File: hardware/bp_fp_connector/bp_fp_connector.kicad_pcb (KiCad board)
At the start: 2 copper layers, 26.3 x 100 mm, 0 parts

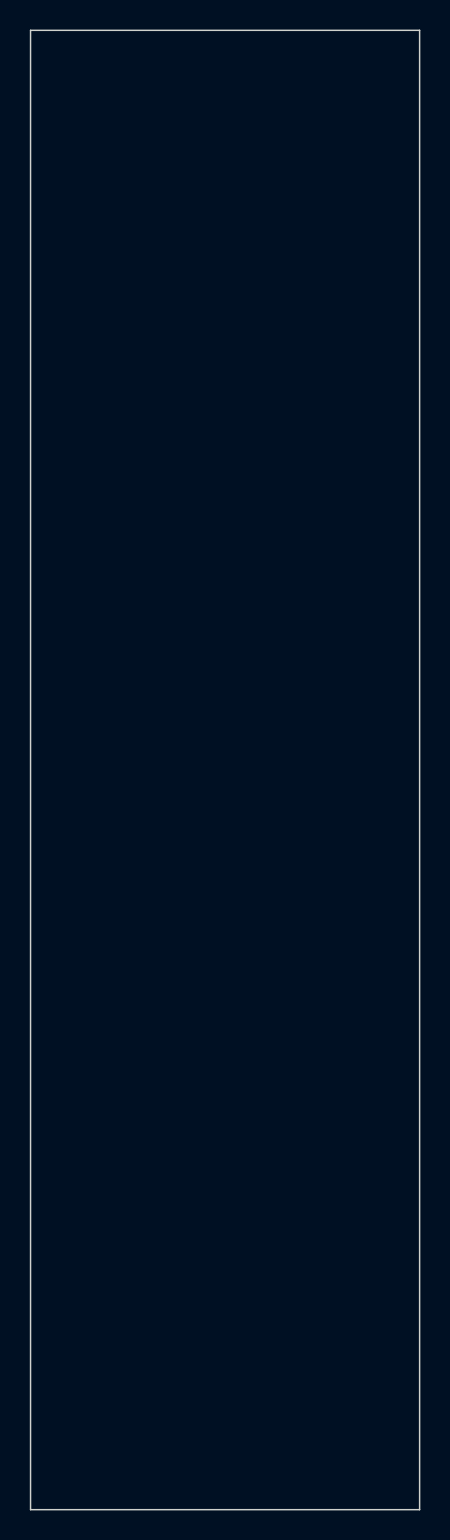
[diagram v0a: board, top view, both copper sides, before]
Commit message: front panel - backplane connector
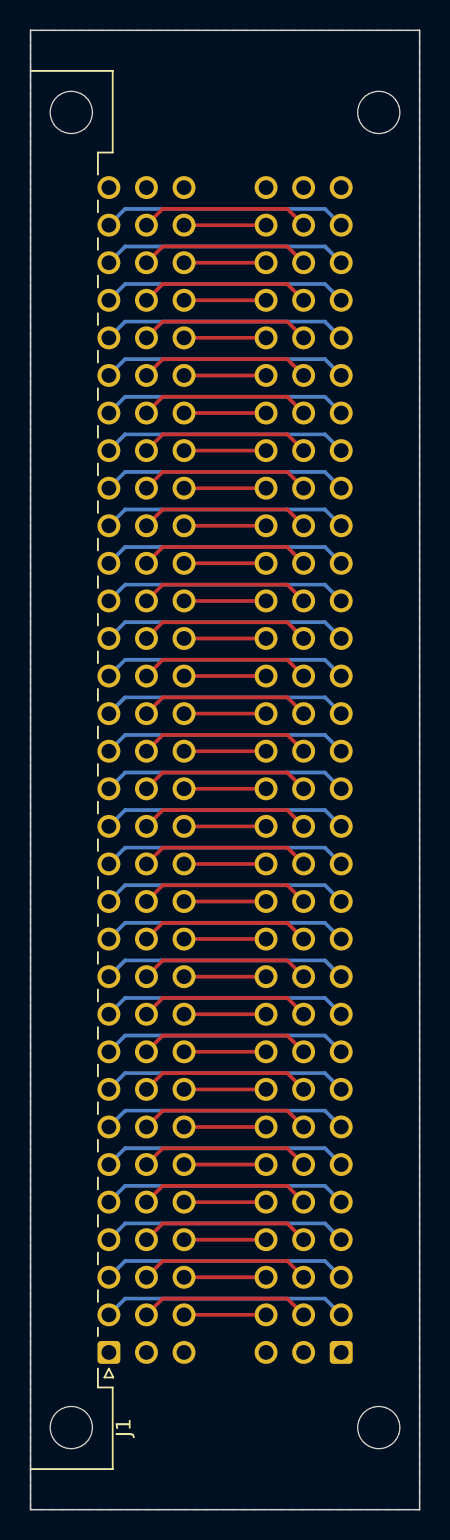
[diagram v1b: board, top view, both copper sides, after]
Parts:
- added J1: C96ABC, din61412:DIN41612_C_3x32_Male_Horizontal_THT_CAPS, F.Cu at (17.3, 101.4)
- added J2: C96ABC, din61412:DIN41612_C_3x32_Male_Horizontal_THT_CAPS, B.Cu at (33.0, 101.4)
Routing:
- net Net-(J1-PadA8): track 0.00 -> 16.6 mm
- net Net-(J1-PadA6): track 0.00 -> 16.6 mm
- net Net-(J1-PadA4): track 0.00 -> 16.6 mm
- net Net-(J1-PadA3): track 0.00 -> 16.6 mm
- net Net-(J1-PadA24): track 0.00 -> 16.6 mm
- net Net-(J1-PadA16): track 0.00 -> 16.6 mm
- net Net-(J1-PadA15): track 0.00 -> 16.6 mm
- net Net-(J1-PadA13): track 0.00 -> 16.6 mm
- net Net-(J1-PadA12): track 0.00 -> 16.6 mm
- net Net-(J1-PadA10): track 0.00 -> 16.6 mm
- net Net-(J1-PadA31): track 0.00 -> 16.6 mm
- net Net-(J1-PadA30): track 0.00 -> 16.6 mm
- net Net-(J1-PadA29): track 0.00 -> 16.6 mm
- net Net-(J1-PadA28): track 0.00 -> 16.6 mm
- net Net-(J1-PadA27): track 0.00 -> 16.6 mm
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- added copper zone on B.Cu, net GND
- added copper zone on F.Cu, net VCC

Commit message: bp_fp connector improvements
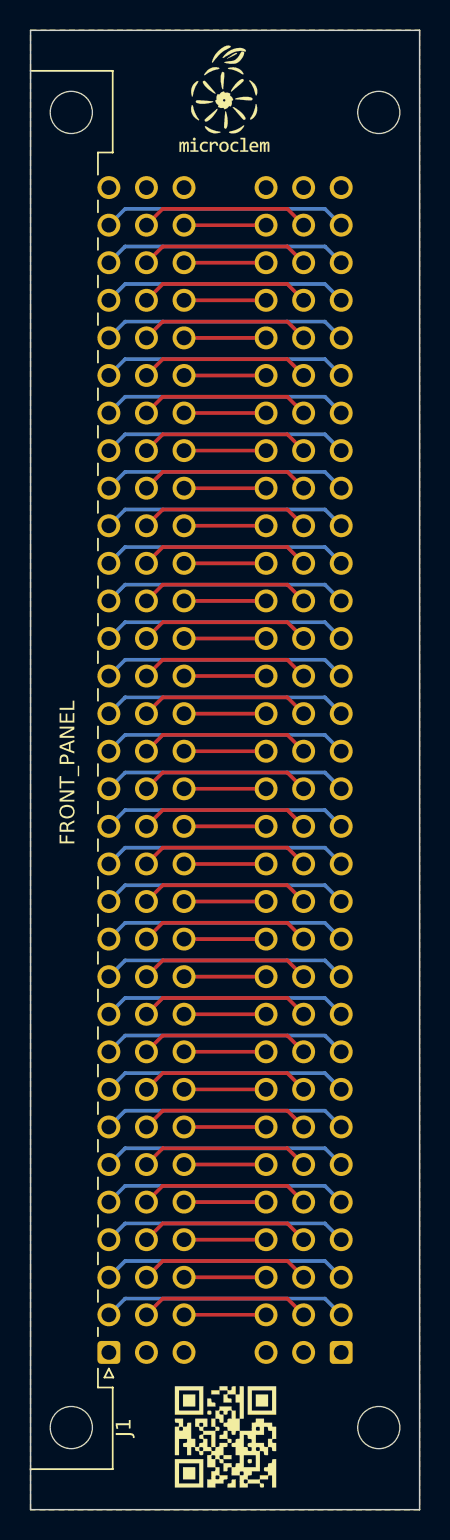
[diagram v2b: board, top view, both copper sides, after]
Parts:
- added G***: LOGO, graphics:qr_code_small, F.Cu at (25.2, 107.1)
- added G***: LOGO, graphics:microclem_logo_silk_screen_small, F.Cu at (25.1, 16.7)
- added G***: LOGO, graphics:microclem_logo_mask_small, B.Cu at (25.1, 16.7)
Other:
- board text added: "BACKPLANE"
- board text added: "FRONT_PANEL"
